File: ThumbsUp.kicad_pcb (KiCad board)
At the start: 2 copper layers, 250.9 x 280.9 mm, 172 parts, among them IC1 RP2040, IC2 W25Q128JVSIM, IC3 RP2040, IC4 W25Q128JVSIM, J1 Conn_01x04_Male, J10 Raiser_Male, J11 Raiser_Female, J12 Raiser_Male, J13 Raiser_Female, J14 Raiser_Male, J15 Raiser_Female, J16 Raiser_Male, J17 Raiser_Female, J18 Raiser_Male, J19 Raiser_Female, J2 Conn_01x04_Male, J20 Conn_01x04_Female, J21 Conn_01x04_Female, J22 Conn_01x04_Female, J23 Conn_01x04_Female, J24 Conn_01x04_Male, J25 Conn_01x04_Male, J26 Conn_01x04_Male, J27 Conn_01x04_Male, J28 Conn_01x04_Female, J29 Conn_01x04_Female, J3 Conn_01x04_Female, J30 Conn_01x04_Female, J31 Conn_01x04_Female, J32 USB_C_Receptacle_USB2.0, J33 Raiser_Male, J34 Raiser_Female, J35 Raiser_Male, J36 STX-3501-3N, J37 USB_C_Receptacle_USB2.0, J38 Raiser_Female, J39 Raiser_Male, J4 Conn_01x04_Male, J40 Raiser_Female, J41 Raiser_Male, J42 Raiser_Female, J43 Raiser_Male, J44 Raiser_Female, J45 Raiser_Male, J46 STX-3501-3N, J47 Raiser_Female, J48 Raiser_Male, J49 Raiser_Female, J5 Conn_01x04_Female, J50 Raiser_Male, J51 Raiser_Female, J52 Raiser_Male, J6 Conn_01x04_Male, J7 Conn_01x04_Male, J8 Conn_01x04_Male, J9 Raiser_Female, U1 NCP1117-3.3_SOT223, U2 NCP1117-3.3_SOT223, Y1 ABLS-12.000MHZ-B4-T, Y2 ABLS-12.000MHZ-B4-T

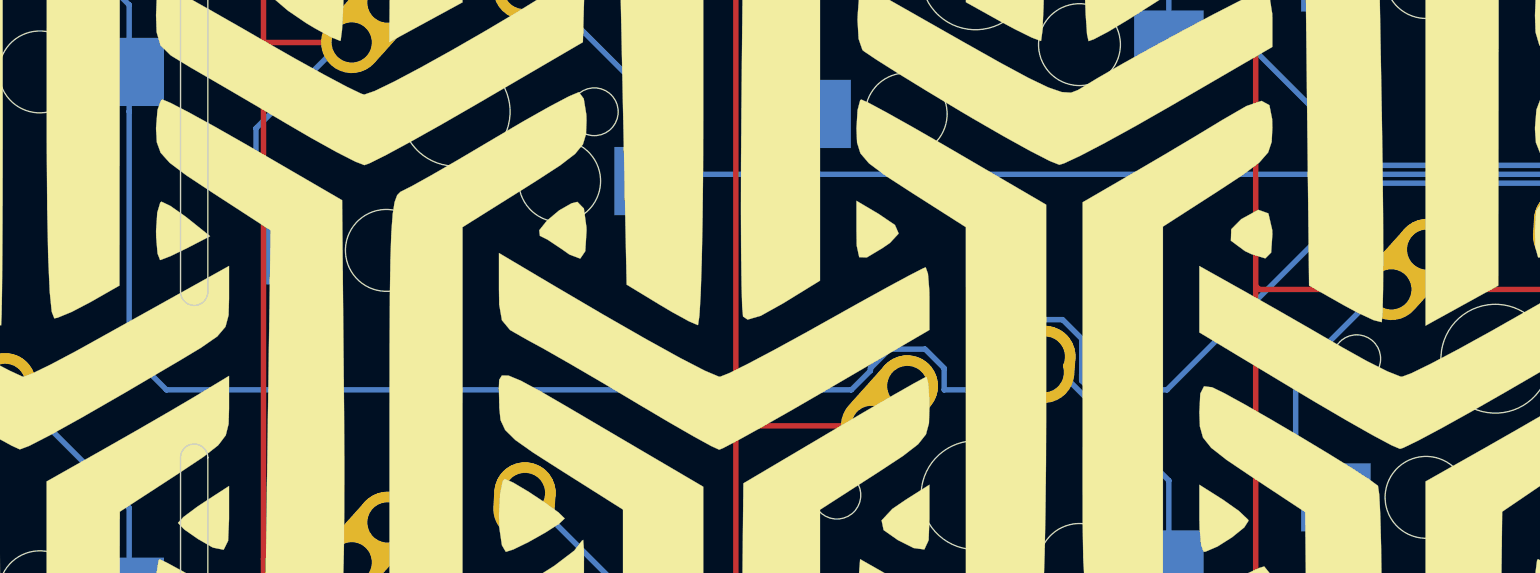
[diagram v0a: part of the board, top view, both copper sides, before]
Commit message: Fixed a line to close to the holes in L3
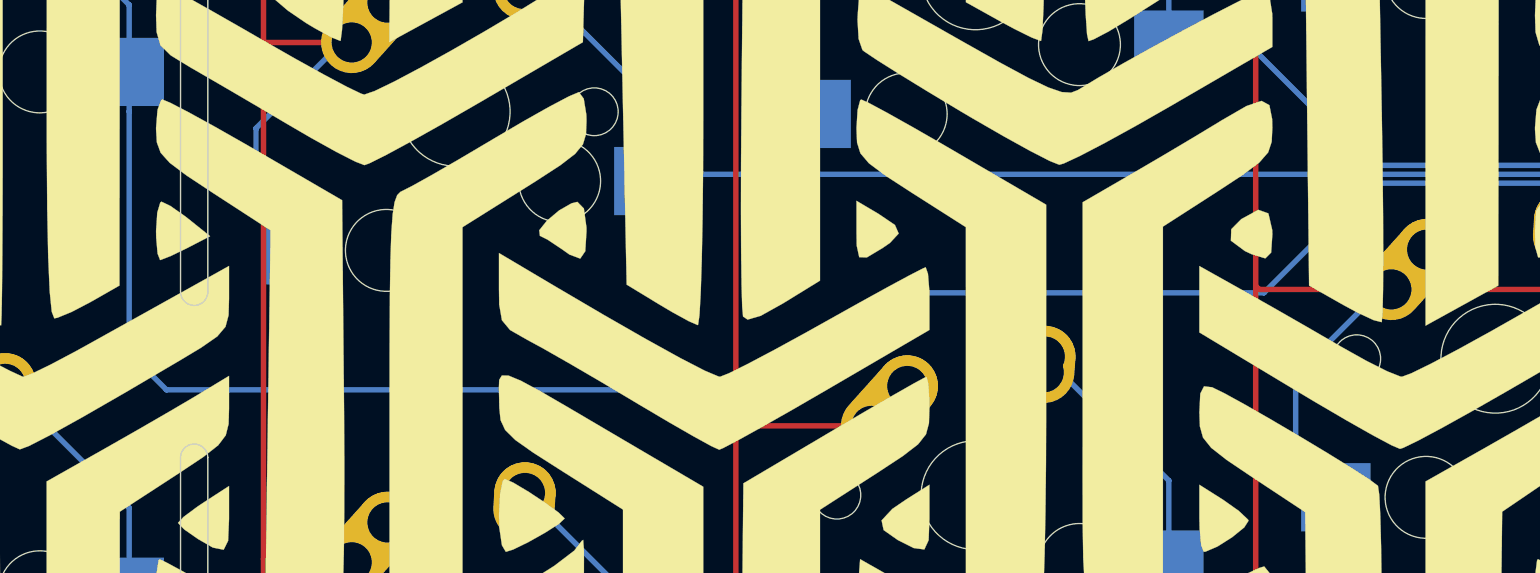
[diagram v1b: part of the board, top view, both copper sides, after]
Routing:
- net Net-(J44-Pad1): track 135.0 -> 129.1 mm
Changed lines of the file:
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@@
     (thickness 1.6)
     (drawings 173)
-    (tracks 2298)
+    (tracks 2281)
     (zones 0)
     (modules 172)
@@
   (segment (start 30.967789 525.047953) (end 30.967789 527.502953) (width 0.2) (layer B.Cu) (net 154))
   (segment (start 26.382789 520.462953) (end 30.967789 525.047953) (width 0.2) (layer B.Cu) (net 154))
-  (segment (start 58.130788 538.363991) (end 58.130788 538.455249) (width 0.2) (layer B.Cu) (net 154))
-  (segment (start 60.13175 537.660951) (end 58.833828 537.660951) (width 0.2) (layer B.Cu) (net 154))
-  (segment (start 60.83479 538.363991) (end 60.13175 537.660951) (width 0.2) (layer B.Cu) (net 154))
-  (segment (start 60.83479 539.154) (end 60.83479 538.363991) (width 0.2) (layer B.Cu) (net 154))
-  (segment (start 30.967789 537.787789) (end 30.967789 528.952953) (width 0.2) (layer B.Cu) (net 154))
-  (segment (start 63.133445 539.075372) (end 63.212073 539.154) (width 0.2) (layer B.Cu) (net 154))
-  (segment (start 63.212073 539.154) (end 60.83479 539.154) (width 0.2) (layer B.Cu) (net 154))
-  (segment (start 68.996 539.154) (end 66.206297 539.154) (width 0.2) (layer B.Cu) (net 154))
-  (segment (start 76.569049 531.580951) (end 68.996 539.154) (width 0.2) (layer B.Cu) (net 154))
-  (segment (start 87.498951 531.580951) (end 76.569049 531.580951) (width 0.2) (layer B.Cu) (net 154))
-  (segment (start 58.833828 537.660951) (end 58.130788 538.363991) (width 0.2) (layer B.Cu) (net 154))
-  (segment (start 63.170788 537.283991) (end 63.170788 537.373191) (width 0.2) (layer B.Cu) (net 154))
-  (segment (start 91.008 535.09) (end 87.498951 531.580951) (width 0.2) (layer B.Cu) (net 154))
-  (segment (start 126.440599 557.344893) (end 104.185706 535.09) (width 0.2) (layer B.Cu) (net 154))
-  (segment (start 104.185706 535.09) (end 91.008 535.09) (width 0.2) (layer B.Cu) (net 154))
-  (segment (start 57.432037 539.154) (end 32.334 539.154) (width 0.2) (layer B.Cu) (net 154))
-  (segment (start 65.872133 538.58457) (end 65.87479 538.581913) (width 0.2) (layer B.Cu) (net 154))
-  (segment (start 66.206297 539.154) (end 65.872133 538.819836) (width 0.2) (layer B.Cu) (net 154))
-  (segment (start 65.87479 538.581913) (end 65.87479 537.283991) (width 0.2) (layer B.Cu) (net 154))
-  (segment (start 65.87479 537.283991) (end 65.17175 536.580951) (width 0.2) (layer B.Cu) (net 154))
   (segment (start 30.967789 528.952953) (end 30.967789 527.502953) (width 0.2) (layer B.Cu) (net 154))
-  (segment (start 65.872133 538.819836) (end 65.872133 538.58457) (width 0.2) (layer B.Cu) (net 154))
-  (segment (start 63.873828 536.580951) (end 63.170788 537.283991) (width 0.2) (layer B.Cu) (net 154))
-  (segment (start 65.17175 536.580951) (end 63.873828 536.580951) (width 0.2) (layer B.Cu) (net 154))
-  (segment (start 58.130788 538.455249) (end 57.432037 539.154) (width 0.2) (layer B.Cu) (net 154))
-  (segment (start 63.133445 537.410534) (end 63.133445 539.075372) (width 0.2) (layer B.Cu) (net 154))
   (segment (start 32.334 539.154) (end 30.967789 537.787789) (width 0.2) (layer B.Cu) (net 154))
-  (segment (start 63.170788 537.373191) (end 63.133445 537.410534) (width 0.2) (layer B.Cu) (net 154))
+  (segment (start 55.194 539.154) (end 32.334 539.154) (width 0.2) (layer B.Cu) (net 154))
+  (segment (start 58.75 535.598) (end 55.194 539.154) (width 0.2) (layer B.Cu) (net 154))
+  (segment (start 104.185706 535.09) (end 91.008 535.09) (width 0.2) (layer B.Cu) (net 154))
+  (segment (start 91.008 535.09) (end 87.498951 531.580951) (width 0.2) (layer B.Cu) (net 154))
+  (segment (start 87.498951 531.580951) (end 76.569049 531.580951) (width 0.2) (layer B.Cu) (net 154))
+  (segment (start 76.569049 531.580951) (end 72.552 535.598) (width 0.2) (layer B.Cu) (net 154))
+  (segment (start 30.967789 537.787789) (end 30.967789 528.952953) (width 0.2) (layer B.Cu) (net 154))
+  (segment (start 126.440599 557.344893) (end 104.185706 535.09) (width 0.2) (layer B.Cu) (net 154))
+  (segment (start 72.552 535.598) (end 58.75 535.598) (width 0.2) (layer B.Cu) (net 154))
   (segment (start 46.052789 524.462952) (end 45.432789 524.462952) (width 0.2) (layer B.Cu) (net 155))
   (segment (start 50.017789 528.427952) (end 46.052789 524.462952) (width 0.2) (layer B.Cu) (net 155))
